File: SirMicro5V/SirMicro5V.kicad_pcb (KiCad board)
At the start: 2 copper layers, 50.8 x 20.3 mm, 35 parts, among them J1 Conn_01x16, J2 Conn_01x16, J3 USB_B_Micro, U1 ATmega32U4-AU, U2 AP2127K-3.3, Y1 Resonator

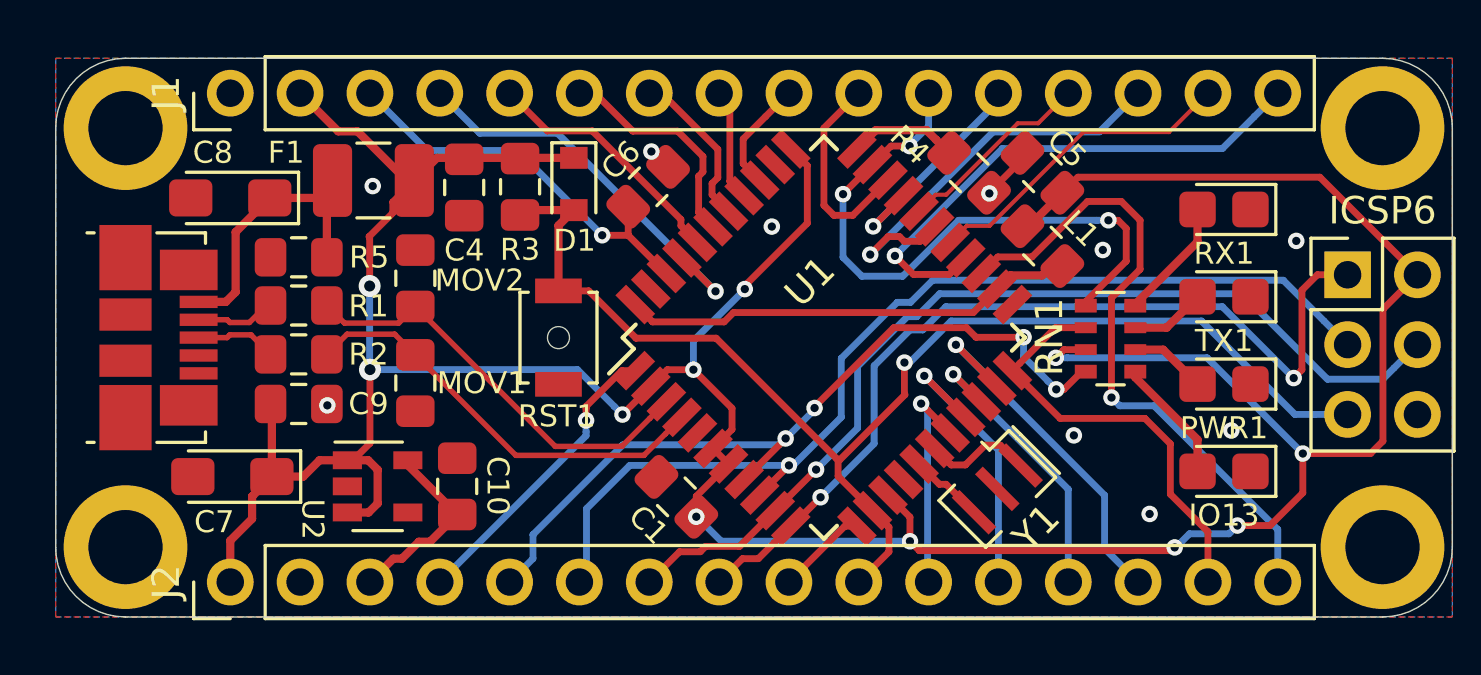
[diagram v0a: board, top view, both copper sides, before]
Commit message: PCB Silkscreen revised
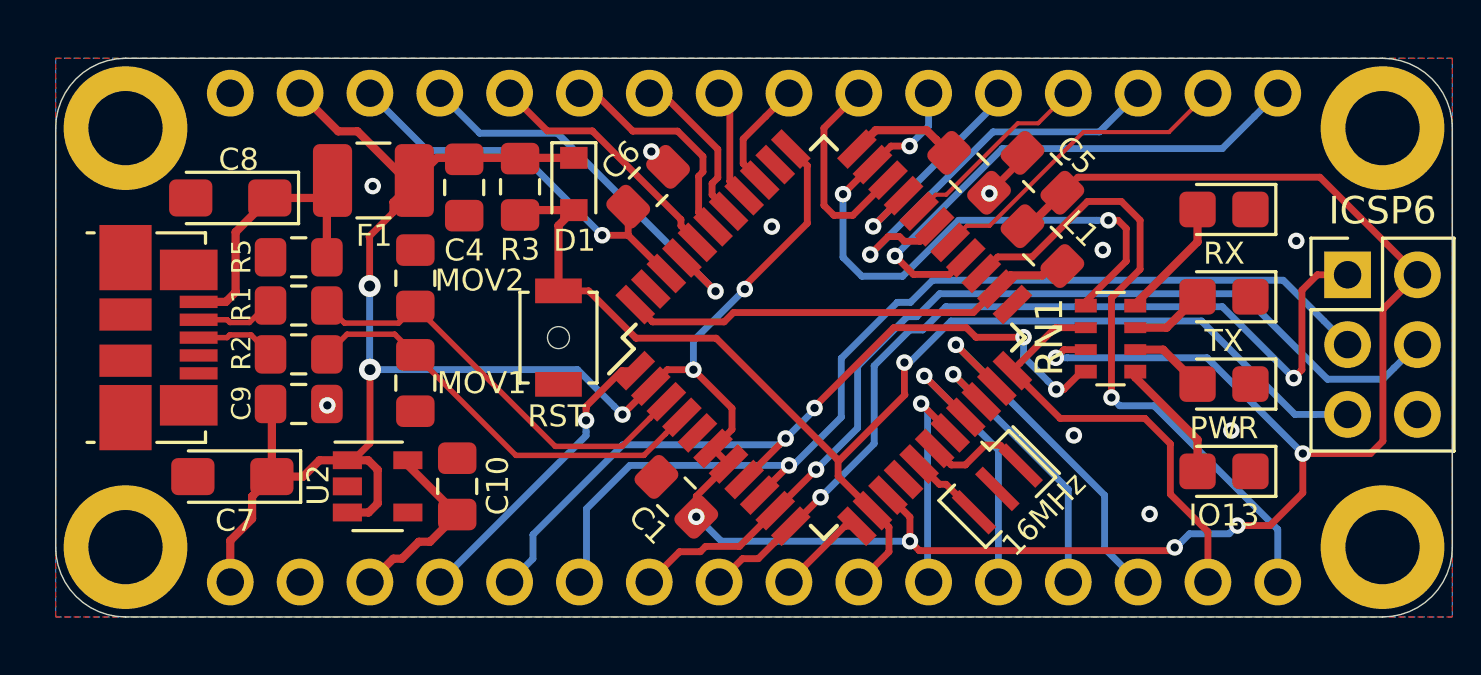
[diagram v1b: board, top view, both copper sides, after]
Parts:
- added G***: LOGO, logo:SirMicro127x42, B.Cu at (233.8, 141.2)
- added G***: LOGO, logo:SirBoard140x44, B.Cu at (212.1, 141.1)
- added G***: LOGO, logo:logo126x178, B.Cu at (203.3, 141.1)
- J1, J2: moved to B.Cu
- turned J1 to 270 degrees
- turned J2 to 270 degrees
- renumbered Y1 to 16MHz, PWR1 to PWR, RST1 to RST, RX1 to RX, TX1 to TX
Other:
- board text added: "16MHz 5V"
- board text added: "8MHz 3.3V"
- board text added: "ATMega32U4 Development Board"
- board text added: "www.SirBoard.com"

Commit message: Board Layout Revised and 3V3 Version Added
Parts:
- added JP1: SolderJumper_2_Bridged, Jumper:SolderJumper-2_P1.3mm_Bridged_RoundedPad1.0x1.5mm, F.Cu at (89.9, 63.4)
- added REF**: OSHW-Logo2_9.8x8mm_SilkScreen, Symbol:OSHW-Logo2_9.8x8mm_SilkScreen, B.Cu at (105.4, 58.3)
- moved C1 151.2 mm to (93.1, 63.6), turned to 180 degrees
- moved C6 150.5 mm to (92.9, 52.5)
- moved REF** 150.4 mm to (119.7, 50.3)
- moved REF** 150.4 mm to (74.0, 50.3)
- moved C9 150.3 mm to (80.3, 60.4)
- moved D1 150.3 mm to (90.3, 52.4)
- moved G*** 150.3 mm to (78.0, 58.1)
- moved IO13 150.3 mm to (114.0, 62.9)
- moved J1 150.3 mm to (77.8, 49.1)
- moved J2 150.3 mm to (77.8, 66.9)
- moved R1 150.3 mm to (80.3, 56.8)
- moved R5 150.3 mm to (80.3, 55.1)
- moved RN1 150.3 mm to (109.8, 58.0)
- moved TX1 150.3 mm to (114.0, 56.5)
- moved Y1 150.3 mm to (105.7, 63.5)
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- renumbered PWR to PWR1, RST to RST1, RX to RX1, TX to TX1, 16MHz to Y1
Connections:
- net +3V3 renamed 3V3
- net /A0 renamed A0
- net /A1 renamed A1
- net /A2 renamed A2
- net /A3 renamed A3
- net /A4 renamed A4
- net /A5 renamed A5
- net /AREF renamed AREF
- net /IO13LED renamed Net-(IO13-Pad2)
- net /MISO renamed MISO
- net /MOSI renamed MOSI
- net /PWRLED renamed Net-(PWR1-Pad2)
- net /RST renamed RST
- net /RXLED renamed Net-(RN1-Pad8)
- net /SCK renamed SCK
- net /TXLED renamed Net-(RN1-Pad7)
- net Net-(J1-Pad10) renamed D5
- net Net-(J1-Pad11) renamed D13
- net Net-(J1-Pad12) renamed D10
- net Net-(J1-Pad13) renamed D9
- net Net-(J1-Pad15) renamed D6
- net Net-(J2-Pad11) renamed SCL
- net Net-(J2-Pad12) renamed SDA
- net Net-(J2-Pad13) renamed RX
- net Net-(J2-Pad14) renamed TX
- net Net-(J2-Pad4) renamed D7
- net Net-(J2-Pad5) renamed RXLED
- C1 pad 1: /5V -> 5V
- C4 pad 1: /5V -> 5V
- C5 pad 1: /5V -> 5V
- C7 pad 1: /5V -> 5V
- C9 pad 1: /5V -> 5V
- D1 pad 1: /5V -> 5V
- F1 pad 1: /5V -> 5V
- ICSP6 pad 2: /5V -> 5V
- J1 pad 14: Net-(J1-Pad14) -> D4
- J1 pad 16: Net-(J1-Pad16) -> D12
- J1 pad 2: /5V -> 5V
- J2 pad 1: /5V -> GND
- J2 pad 15: Net-(J2-Pad15) -> TXLED
- J2 pad 16: Net-(J2-Pad16) -> D8
- J2 pad 2: GND -> 5V
- J2 pad 9: Net-(J2-Pad9) -> D12
- L1 pad 1: /5V -> 5V
- R3 pad 1: /5V -> 5V
- RN1 pad 2: Net-(J2-Pad15) -> 5V
- RN1 pad 3: /5V -> TXLED
- U1 pad 12: Net-(J2-Pad9) -> D11
- U1 pad 14: /5V -> 5V
- U1 pad 2: /5V -> 5V
- U1 pad 22: Net-(J2-Pad15) -> TXLED
- U1 pad 25: Net-(J2-Pad16) -> D4
- U1 pad 26: Net-(J1-Pad16) -> D12
- U1 pad 28: Net-(J1-Pad14) -> D8
- U1 pad 34: /5V -> 5V
- U1 pad 6: /5V -> 5V
- U1 pad 7: /5V -> 5V
- U2 pad 1: /5V -> 5V
- U2 pad 3: /5V -> 5V
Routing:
- net /5V: track 131.6 -> 0.00 mm, vias 11 -> 0
- net 5V: track 0.00 -> 120.1 mm, vias 0 -> 7
- net D12: track 0.00 -> 34.8 mm, vias 0 -> 5
- net Net-(J2-Pad16): track 24.0 -> 0.00 mm, vias 1 -> 0
- net D8: track 0.00 -> 23.1 mm
- net Net-(J1-Pad16): track 19.5 -> 0.00 mm, vias 1 -> 0
- net Net-(J2-Pad15): track 15.8 -> 0.00 mm
- net Net-(J1-Pad14): track 15.1 -> 0.00 mm, vias 1 -> 0
- net TXLED: track 0.00 -> 14.7 mm, vias 0 -> 2
- net D4: track 0.00 -> 10.3 mm, vias 0 -> 1
- net AREF: track 14.5 -> 24.3 mm, vias 1 -> 2
- net SCK: track 37.6 -> 31.2 mm
- net TX: track 13.5 -> 9.25 mm, vias 1 -> 0
- net D13: track 22.6 -> 18.9 mm, vias 3 -> 1
- net A5: track 14.7 -> 11.3 mm
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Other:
- board size 50.8 x 20.3 mm -> 50.8 x 20.5 mm
- board text added: "3V3"
- board text added: "5V"
- board text added: "A0"
- board text added: "A1"
- board text added: "A2"
- board text added: "A3"
- board text added: "A4"
- board text added: "A5"
- board text added: "AREF"
- board text added: "D10"
- board text added: "D12"
- board text added: "D13"
- board text added: "D5"
- board text added: "D6"
- board text added: "D7"
- board text added: "D8"
- board text added: "D9"
- board text added: "GND"
- board text added: "MISO"
- board text added: "MOSI"
- board text added: "PB0"
- board text added: "PD5"
- board text added: "RST"
- board text added: "RX"
- board text added: "SCK"
- board text added: "SCL"
- board text added: "SDA"
- board text added: "TX"

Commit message: Jumper Edited
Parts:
- renumbered Y1 to 16MHz, PWR1 to PWR, RST1 to RST, RX1 to RX, TX1 to TX
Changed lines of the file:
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@@
     (35 F.Paste user hide)
     (36 B.SilkS user)
-    (37 F.SilkS user hide)
+    (37 F.SilkS user)
     (38 B.Mask user hide)
     (39 F.Mask user hide)
@@
     (add_net TXLED)
   )
+  (module Jumper:SolderJumper-2_P1.3mm_Bridged_RoundedPad1.0x1.5mm (layer F.Cu)
+    (at 89.8652 63.4238)
+    (descr "SMD Solder Jumper, 1x1.5mm, rounded Pads, 0.3mm gap, bridged with 1 copper strip")
+    (tags "solder jumper open")
+    (attr virtual)
+    (fp_text reference JP1 (at 0.0254 1.651) (layer F.SilkS)
+      (effects (font (size 0.8 0.8) (thickness 0.12)))
+    )
+    (fp_text value SolderJumper_2_Bridged (at 0 1.9) (layer F.Fab)
+      (effects (font (size 1 1) (thickness 0.15)))
+    )
+    (fp_poly (pts (xy 0.25 -0.127) (xy -0.25 -0.127) (xy -0.25 0.127) (xy 0.25 0.127)) (layer F.Cu) (width 0))
+    (fp_line (start 1.65 1.25) (end -1.65 1.25) (layer F.CrtYd) (width 0.05))
+    (fp_line (start 1.65 1.25) (end 1.65 -1.25) (layer F.CrtYd) (width 0.05))
+    (fp_line (start -1.65 -1.25) (end -1.65 1.25) (layer F.CrtYd) (width 0.05))
+    (fp_line (start -1.65 -1.25) (end 1.65 -1.25) (layer F.CrtYd) (width 0.05))
+    (fp_line (start -0.7 -1) (end 0.7 -1) (layer F.SilkS) (width 0.12))
+    (fp_line (start 1.4 -0.3) (end 1.4 0.3) (layer F.SilkS) (width 0.12))
+    (fp_line (start 0.7 1) (end -0.7 1) (layer F.SilkS) (width 0.12))
+    (fp_line (start -1.4 0.3) (end -1.4 -0.3) (layer F.SilkS) (width 0.12))
+    (fp_arc (start -0.7 -0.3) (end -0.7 -1) (angle -90) (layer F.SilkS) (width 0.12))
+    (fp_arc (start -0.7 0.3) (end -1.4 0.3) (angle -90) (layer F.SilkS) (width 0.12))
+    (fp_arc (start 0.7 0.3) (end 0.7 1) (angle -90) (layer F.SilkS) (width 0.12))
+    (fp_arc (start 0.7 -0.3) (end 1.4 -0.3) (angle -90) (layer F.SilkS) (width 0.12))
+    (fp_poly (pts (xy 0.25 -0.127) (xy -0.25 -0.127) (xy -0.25 0.127) (xy 0.25 0.127)) (layer F.Mask) (width 0))
+    (pad 1 smd custom (at -0.65 0) (size 1 0.5) (layers F.Cu F.Mask)
+      (net 13 5V) (zone_connect 2)
+      (options (clearance outline) (anchor rect))
+      (primitives
+        (gr_circle (center 0 0.25) (end 0.5 0.25) (width 0))
+        (gr_circle (center 0 -0.25) (end 0.5 -0.25) (width 0))
+        (gr_poly (pts
+           (xy 0 -0.75) (xy 0.5 -0.75) (xy 0.5 0.75) (xy 0 0.75)) (width 0))
+      ))
+    (pad 2 smd custom (at 0.65 0) (size 1 0.5) (layers F.Cu F.Mask)
+      (net 14 AREF) (zone_connect 2)
+      (options (clearance outline) (anchor rect))
+      (primitives
+        (gr_circle (center 0 0.25) (end 0.5 0.25) (width 0))
+        (gr_circle (center 0 -0.25) (end 0.5 -0.25) (width 0))
+        (gr_poly (pts
+           (xy 0 -0.75) (xy -0.5 -0.75) (xy -0.5 0.75) (xy 0 0.75)) (width 0))
+      ))
+  )
   (module Connector_PinHeader_2.54mm:PinHeader_1x16_P2.54mm_Vertical (layer B.Cu)
     (at 77.8256 66.8782 270)
@@
       (rotate (xyz 0 0 0))
     )
-  )
-  (module Jumper:SolderJumper-2_P1.3mm_Bridged_RoundedPad1.0x1.5mm (layer F.Cu)
-    (at 89.8652 63.4238)
-    (descr "SMD Solder Jumper, 1x1.5mm, rounded Pads, 0.3mm gap, bridged with 1 copper strip")
-    (tags "solder jumper open")
-    (attr virtual)
-    (fp_text reference JP1 (at 0.0254 1.651) (layer F.SilkS)
-      (effects (font (size 0.8 0.8) (thickness 0.12)))
-    )
-    (fp_text value SolderJumper_2_Bridged (at 0 1.9) (layer F.Fab)
-      (effects (font (size 1 1) (thickness 0.15)))
-    )
-    (fp_poly (pts (xy 0.25 -0.3) (xy -0.25 -0.3) (xy -0.25 0.3) (xy 0.25 0.3)) (layer F.Cu) (width 0))
-    (fp_line (start 1.65 1.25) (end -1.65 1.25) (layer F.CrtYd) (width 0.05))
-    (fp_line (start 1.65 1.25) (end 1.65 -1.25) (layer F.CrtYd) (width 0.05))
-    (fp_line (start -1.65 -1.25) (end -1.65 1.25) (layer F.CrtYd) (width 0.05))
-    (fp_line (start -1.65 -1.25) (end 1.65 -1.25) (layer F.CrtYd) (width 0.05))
-    (fp_line (start -0.7 -1) (end 0.7 -1) (layer F.SilkS) (width 0.12))
-    (fp_line (start 1.4 -0.3) (end 1.4 0.3) (layer F.SilkS) (width 0.12))
-    (fp_line (start 0.7 1) (end -0.7 1) (layer F.SilkS) (width 0.12))
-    (fp_line (start -1.4 0.3) (end -1.4 -0.3) (layer F.SilkS) (width 0.12))
-    (fp_arc (start -0.7 -0.3) (end -0.7 -1) (angle -90) (layer F.SilkS) (width 0.12))
-    (fp_arc (start -0.7 0.3) (end -1.4 0.3) (angle -90) (layer F.SilkS) (width 0.12))
-    (fp_arc (start 0.7 0.3) (end 0.7 1) (angle -90) (layer F.SilkS) (width 0.12))
-    (fp_arc (start 0.7 -0.3) (end 1.4 -0.3) (angle -90) (layer F.SilkS) (width 0.12))
-    (pad 1 smd custom (at -0.65 0) (size 1 0.5) (layers F.Cu F.Mask)
-      (net 13 5V) (zone_connect 2)
-      (options (clearance outline) (anchor rect))
-      (primitives
-        (gr_circle (center 0 0.25) (end 0.5 0.25) (width 0))
-        (gr_circle (center 0 -0.25) (end 0.5 -0.25) (width 0))
-        (gr_poly (pts
-           (xy 0 -0.75) (xy 0.5 -0.75) (xy 0.5 0.75) (xy 0 0.75)) (width 0))
-      ))
-    (pad 2 smd custom (at 0.65 0) (size 1 0.5) (layers F.Cu F.Mask)
-      (net 14 AREF) (zone_connect 2)
-      (options (clearance outline) (anchor rect))
-      (primitives
-        (gr_circle (center 0 0.25) (end 0.5 0.25) (width 0))
-        (gr_circle (center 0 -0.25) (end 0.5 -0.25) (width 0))
-        (gr_poly (pts
-           (xy 0 -0.75) (xy -0.5 -0.75) (xy -0.5 0.75) (xy 0 0.75)) (width 0))
-      ))
   )
   (module Symbol:OSHW-Logo2_9.8x8mm_SilkScreen (layer B.Cu)
@@
     (tags "SMD SMT ceramic resonator filter")
     (attr smd)
-    (fp_text reference Y1 (at -0.54217 -1.849933 45) (layer F.SilkS)
+    (fp_text reference 16MHz (at -1.278551 -1.867893 45) (layer F.SilkS)
       (effects (font (size 0.8 0.8) (thickness 0.13)))
     )
@@
     (tags "LED castellated")
     (attr smd)
-    (fp_text reference RX1 (at 0 -1.6) (layer F.SilkS)
+    (fp_text reference RX (at 0 -1.6) (layer F.SilkS)
       (effects (font (size 0.8 0.8) (thickness 0.15)))
     )
@@
     (tags "LED castellated")
     (attr smd)
-    (fp_text reference PWR1 (at 0 -1.6) (layer F.SilkS)
+    (fp_text reference PWR (at 0 -1.6) (layer F.SilkS)
       (effects (font (size 0.8 0.8) (thickness 0.15)))
     )
@@
     (tags "LED castellated")
     (attr smd)
-    (fp_text reference TX1 (at 0 -1.6) (layer F.SilkS)
+    (fp_text reference TX (at 0 -1.6) (layer F.SilkS)
       (effects (font (size 0.8 0.8) (thickness 0.15)))
     )
@@
     (tags "Tactile Switch")
     (attr smd)
-    (fp_text reference RST1 (at -2.8575 -0.0635 180) (layer F.SilkS)
+    (fp_text reference RST (at -2.8575 -0.0635 180) (layer F.SilkS)
       (effects (font (size 0.8 0.8) (thickness 0.15)))
     )

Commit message: Dual Voltage And Voltage Selector Added, QFN Package used
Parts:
- renumbered PWR to PWR1, RST to RST1, RX to RX1, TX to TX1, 16MHz to Y1
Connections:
- C1 pad 1: 5V -> Net-(C1-Pad1)
- U1 pad 6: 5V -> Net-(C1-Pad1)
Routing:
- net Net-(C1-Pad1): track 0.00 -> 2.11 mm, vias 0 -> 1
- net 5V: track 120.1 -> 121.0 mm
